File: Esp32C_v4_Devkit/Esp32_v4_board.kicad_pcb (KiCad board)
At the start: 2 copper layers, 28 x 54.5 mm, 34 parts, among them J1 USB_CON8, J2 Conn_01x19_Male, J3 Conn_01x19_Male, Q1 SS8O5O-G, Q2 SS8O5O-G, SW1 SW_Push, SW2 SW_Push, U1 CP2102N-A01-GQFN28, U2 AMS117_3.3

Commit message: Routing and components placement
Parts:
- moved J2 45.8 mm to (127.0, 75.6), turned to 180 degrees
- moved J3 45.8 mm to (151.9, 75.7), turned to 180 degrees
- moved R25 22.8 mm to (144.9, 116.2), turned to 270 degrees
- moved D6 21.9 mm to (137.2, 116.5), turned to 270 degrees
- moved R23 20.9 mm to (148.9, 119.3), turned to 90 degrees
- moved C9 20.9 mm to (131.4, 96.2), turned to 90 degrees
- moved Q1 20.1 mm to (131.4, 115.3), turned to 180 degrees
- moved C21 19.7 mm to (140.8, 97.0), turned to 270 degrees
- moved C14 19.6 mm to (129.8, 96.3), turned to 180 degrees
- moved D5 18.1 mm to (140.8, 116.5), turned to 270 degrees
- moved C19 17.3 mm to (138.3, 98.2), turned to 90 degrees
- moved C22 16.8 mm to (136.2, 98.2), turned to 270 degrees
- moved C3 16.3 mm to (143.7, 97.1), turned to 270 degrees
- moved R26 15.2 mm to (147.8, 116.2), turned to 90 degrees
- moved SW2 14.9 mm to (132.2, 120.4)
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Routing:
- net GND: track 0.00 -> 166.3 mm, vias 0 -> 4
- net +3V3: track 0.00 -> 81.4 mm, vias 0 -> 5
- net /EN: track 0.00 -> 57.1 mm, vias 0 -> 3
- net /IO0: track 0.00 -> 49.3 mm, vias 0 -> 2
- net /CMD: track 0.00 -> 45.9 mm, vias 0 -> 1
- net /CLK: track 0.00 -> 43.7 mm, vias 0 -> 1
- net /SD3: track 0.00 -> 39.5 mm, vias 0 -> 1
- net /SD0: track 0.00 -> 39.0 mm, vias 0 -> 1
- net /SD1: track 0.00 -> 35.2 mm, vias 0 -> 1
- net /RXD0: track 0.00 -> 35.1 mm, vias 0 -> 2
- net /SD2: track 0.00 -> 34.2 mm, vias 0 -> 1
- net +5V: track 0.00 -> 33.7 mm, vias 0 -> 1
- net /TXD0: track 0.00 -> 33.4 mm, vias 0 -> 2
- net /IO15: track 0.00 -> 31.9 mm, vias 0 -> 1
- net /IO2: track 0.00 -> 27.5 mm, vias 0 -> 1
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
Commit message: Routing and components placement
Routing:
- net GND: track 166.3 -> 137.5 mm
- added copper zone on B.Cu, net GND
- added copper zone on F.Cu, net GND

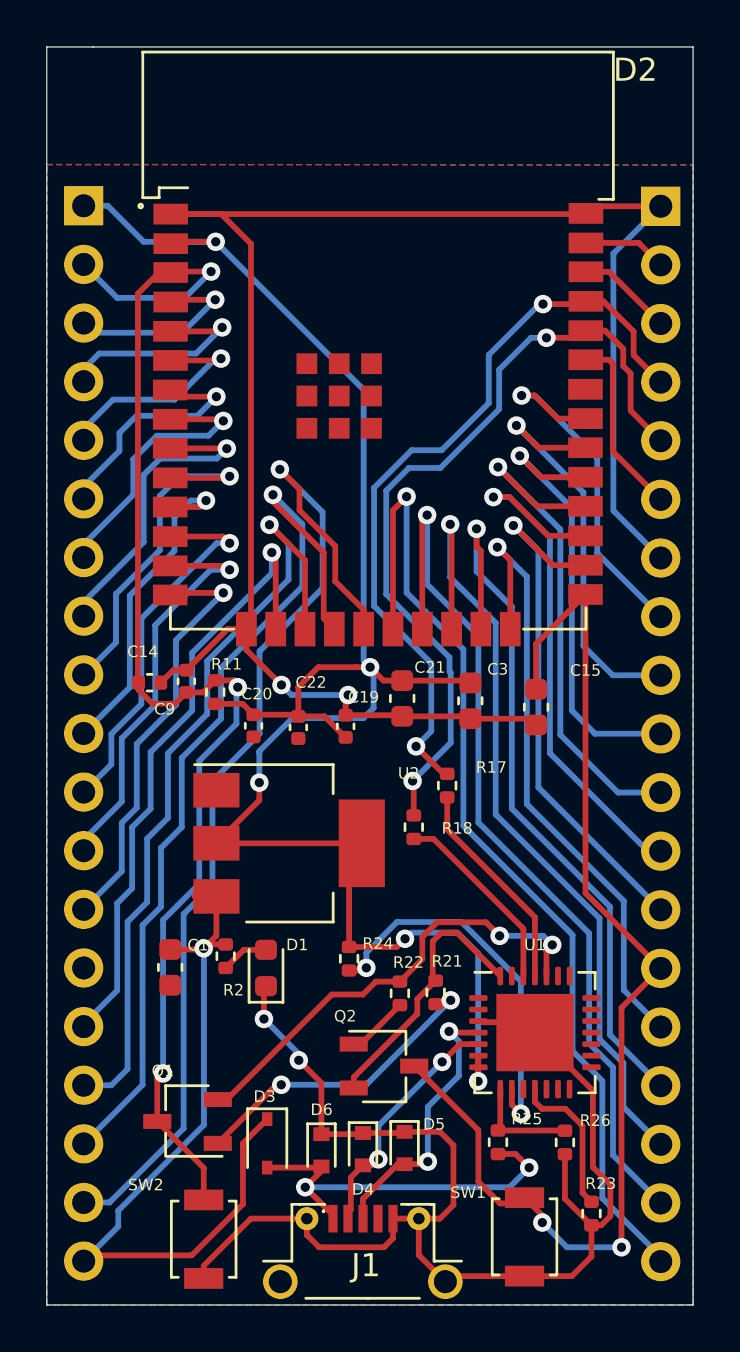
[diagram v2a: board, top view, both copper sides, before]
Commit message: Updated routing corrections
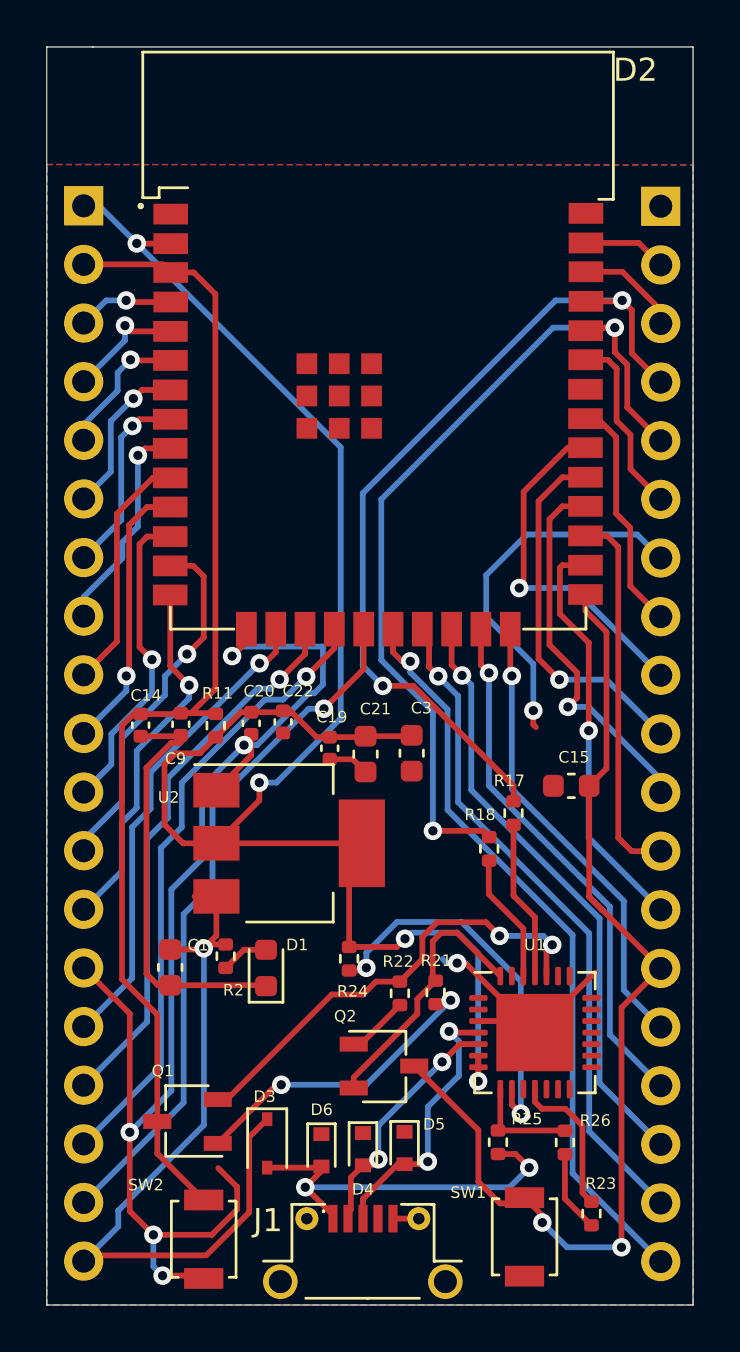
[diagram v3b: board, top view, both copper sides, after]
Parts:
- moved C15 3.74 mm to (148.1, 100.8), turned to 0 degrees
- moved C3 3.41 mm to (141.2, 99.3)
- moved R18 3.40 mm to (144.5, 103.5)
- moved R17 3.11 mm to (145.6, 101.9)
- moved C21 2.89 mm to (139.2, 99.4)
- moved C14 1.88 mm to (129.4, 98.1), turned to 90 degrees
- moved C9 1.88 mm to (131.2, 98.1), turned to 270 degrees
- moved R11 1.45 mm to (132.7, 98.2)
- moved C19 1.17 mm to (137.6, 99.1), turned to 270 degrees
- moved C22 0.70 mm to (135.6, 98.0)
- moved C20 0.15 mm to (134.2, 98.0)
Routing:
- net GND: track 137.5 -> 109.6 mm, vias 4 -> 7
- net /CMD: track 45.9 -> 30.3 mm
- net /SD3: track 39.5 -> 27.3 mm
- net /CLK: track 43.7 -> 32.4 mm
- net /SD2: track 34.2 -> 24.1 mm
- net /SD0: track 39.0 -> 29.1 mm
- net /SD1: track 35.2 -> 26.1 mm
- net /IO15: track 31.9 -> 23.0 mm
- net /IO2: track 27.5 -> 19.9 mm
- net /IO16: track 23.8 -> 16.3 mm, vias 1 -> 0
- net /IO13: track 27.3 -> 20.8 mm
- net /IO17: track 22.6 -> 16.5 mm
- net /EN: track 57.1 -> 51.6 mm, vias 3 -> 0
- net /IO4: track 23.1 -> 17.8 mm
- net /IO19: track 15.6 -> 10.4 mm, vias 1 -> 0
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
